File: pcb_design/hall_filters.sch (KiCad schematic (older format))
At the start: 9 parts

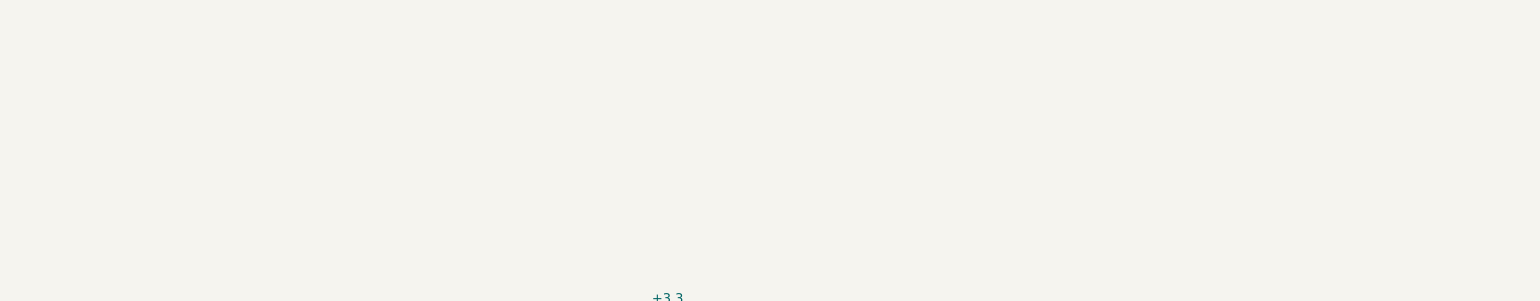
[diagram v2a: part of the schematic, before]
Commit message: Added RC filter to FAULT line to prevent noise triggering it
Signed-off-by: Marcos Chaparro <mchaparro@paltatech.com>
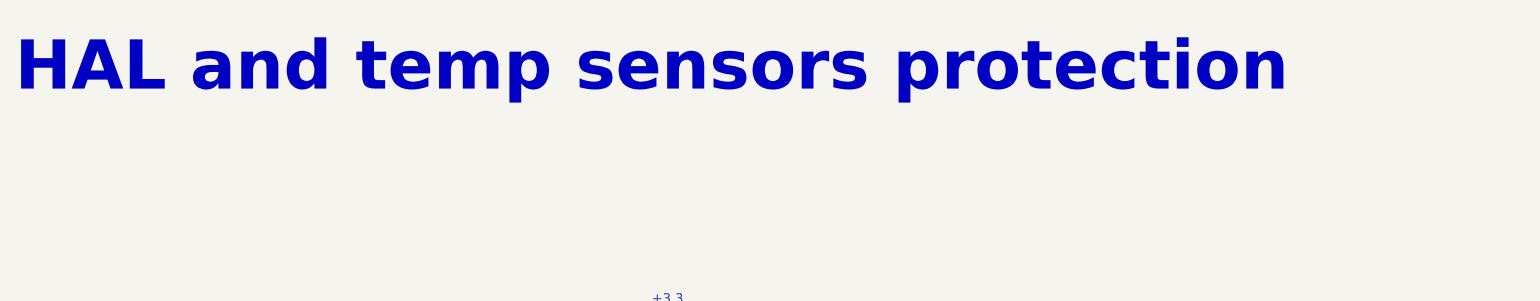
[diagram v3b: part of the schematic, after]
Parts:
- C4: BOM CAP MLCC 4.7nF X7R 50V 10% [0603] -> CAP MLCC 100pF C0G 50V 5% [0603]; mfg# GRM188R71H472KA01D -> (none)
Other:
- note added: "HAL and temp sensors protection"
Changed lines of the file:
@@
 F 2 "IPC7351-Nominal:CAPC1608X55" H 5100 4150 50  0001 C CNN
 F 3 "http://www.murata.com/~/media/webrenewal/support/library/catalog/products/capacitor/mlcc/c02e.ashx" H 5090 4125 60  0001 C CNN
-F 4 "GRM188R71H472KA01D" H 5100 4150 60  0001 C CNN "mfg#"
-F 5 "CAP MLCC 4.7nF X7R 50V 10% [0603]" H 5900 4700 60  0001 C CNN "BOM"
+F 4 "" H 5100 4150 60  0001 C CNN "mfg#"
+F 5 "CAP MLCC 100pF C0G 50V 5% [0603]" H 5900 4700 60  0001 C CNN "BOM"
 F 6 "Murata Electronics North America" H 0   0   50  0001 C CNN "MFR"
 F 7 "GRM188R71A225KE15D" H 0   0   50  0001 C CNN "MPN"
@@
 Connection ~ 6950 3750
 Connection ~ 7450 3850
+Text Notes 1450 1950 0    260  ~ 52
+HAL and temp sensors protection
 $EndSCHEMATC
